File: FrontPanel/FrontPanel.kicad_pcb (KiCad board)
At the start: 2 copper layers, 66 parts, among them SW1 Channel 1, SW10 5, SW11 2, SW12 0, SW13 9, SW14 6, SW15 3, SW16 Backspace, SW17 Voltage 1, SW18 Current 1, SW19 Voltage 2, SW2 Confirm, SW20 Current 2, SW3 Cancel, SW4 Channel 2, SW5 7, SW6 4, SW7 1, SW8 Decimal, SW9 8

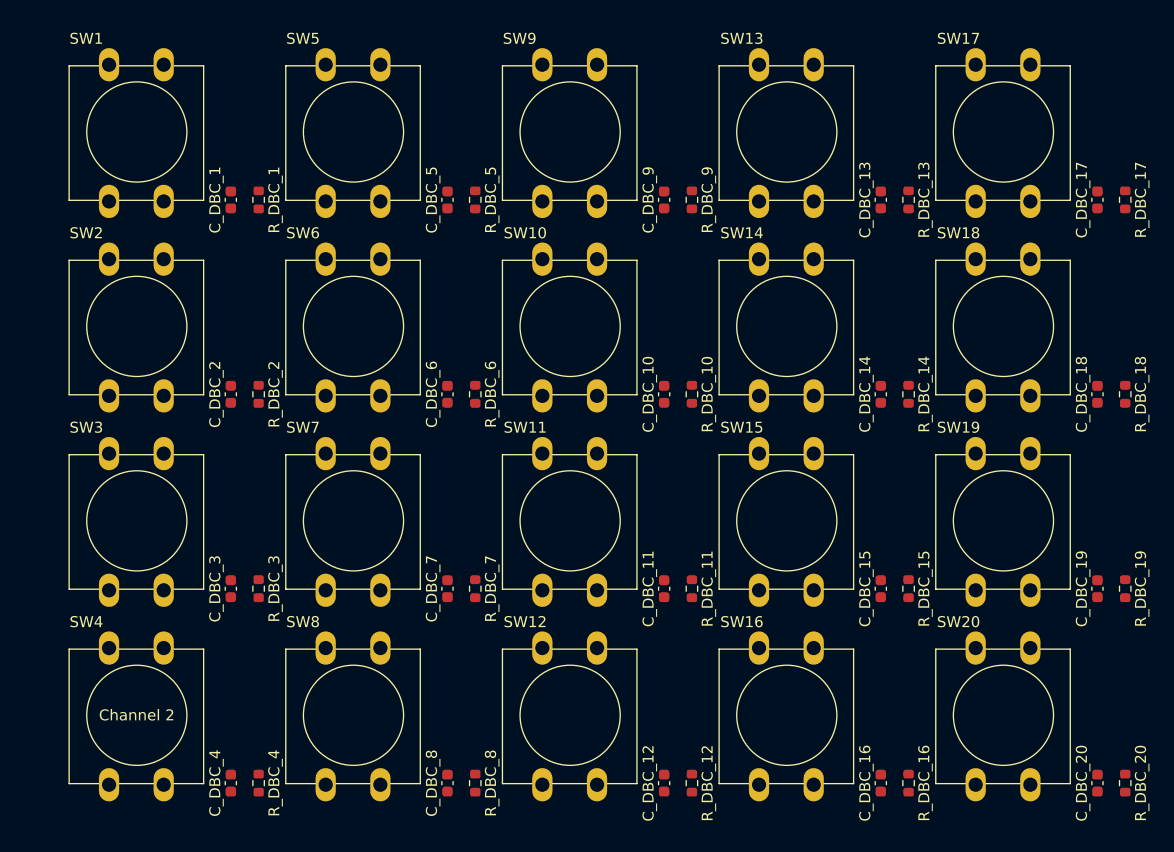
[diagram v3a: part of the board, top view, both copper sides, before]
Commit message: Compressed keypad
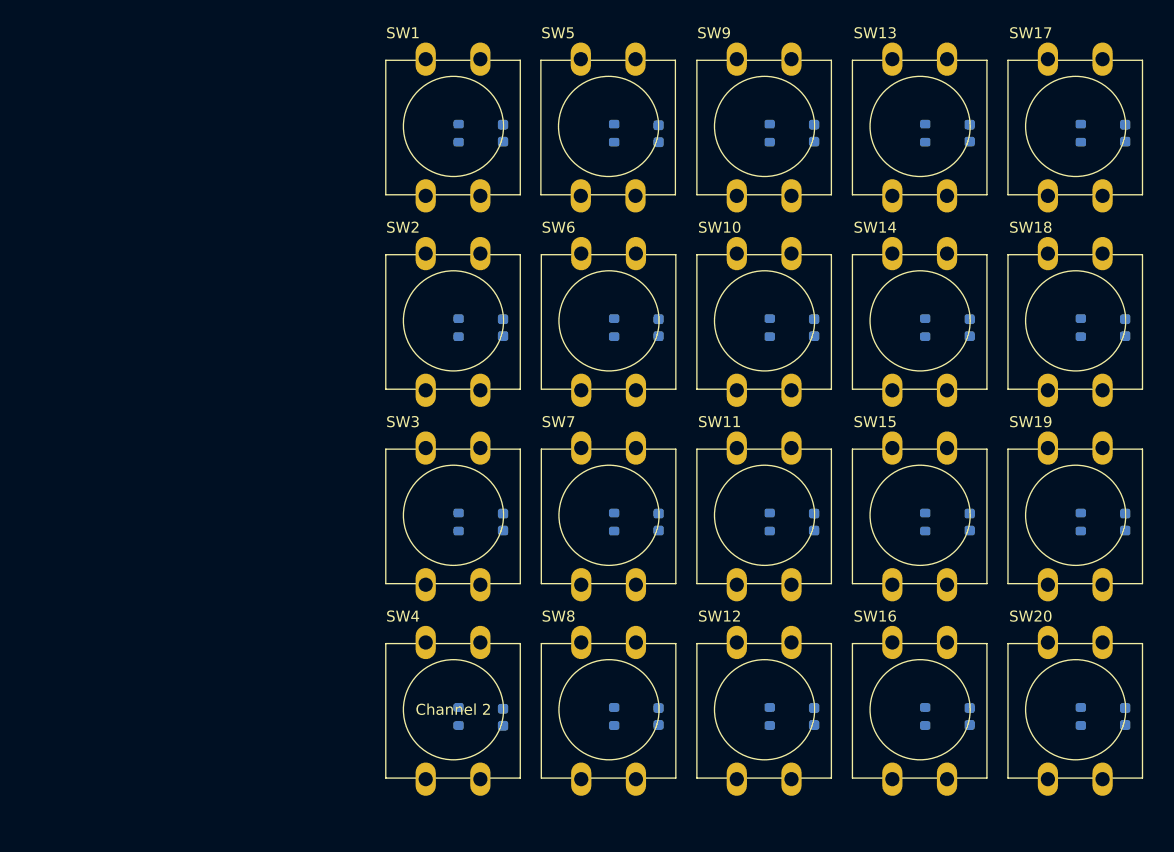
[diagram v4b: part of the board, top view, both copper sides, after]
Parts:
- C_DBC_1, C_DBC_10, C_DBC_11, C_DBC_12, C_DBC_13, C_DBC_14, C_DBC_15, C_DBC_16, C_DBC_17, C_DBC_18, C_DBC_19, C_DBC_2, C_DBC_20, C_DBC_3, C_DBC_4, C_DBC_5, C_DBC_6, C_DBC_7, C_DBC_8, C_DBC_9, R_DBC_1, R_DBC_10, R_DBC_11, R_DBC_12, R_DBC_13, R_DBC_14, R_DBC_15, R_DBC_16, R_DBC_17, R_DBC_18, R_DBC_19, R_DBC_2, R_DBC_20, R_DBC_3, R_DBC_4, R_DBC_5, R_DBC_6, R_DBC_7, R_DBC_8, R_DBC_9: moved to B.Cu
- moved SW1 29.0 mm to (215.9, 29.6)
- moved SW2 29.0 mm to (215.9, 47.4)
- moved SW3 29.0 mm to (215.9, 65.2)
- moved SW4 29.0 mm to (215.9, 82.9)
- moved C_DBC_1 25.6 mm to (223.0, 23.9), turned to -90 degrees
- moved C_DBC_2 25.6 mm to (223.0, 41.7), turned to -90 degrees
- moved C_DBC_3 25.6 mm to (223.0, 59.4), turned to -90 degrees
- moved C_DBC_4 25.6 mm to (223.0, 77.3), turned to -90 degrees
- moved SW6 23.4 mm to (230.2, 47.4)
- moved SW7 23.4 mm to (230.2, 65.2)
- moved SW8 23.4 mm to (230.2, 82.9)
- moved SW5 23.3 mm to (230.1, 29.6)
- moved C_DBC_6 20.2 mm to (237.2, 41.7), turned to -90 degrees
- moved C_DBC_8 20.2 mm to (237.2, 77.2), turned to -90 degrees
- moved C_DBC_7 20.2 mm to (237.2, 59.4), turned to -90 degrees
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
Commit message: Front Panel
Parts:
- removed R1_LED1, R1_LED2: 100, Resistor_SMD:R_0603_1608Metric
- added C_DBC_21: 100n, Capacitor_SMD:C_0603_1608Metric, B.Cu at (186.8, 47.4)
- added C_DBC_22: 100n, Capacitor_SMD:C_0603_1608Metric, B.Cu at (186.8, 52.5)
- added C_DBC_23: 100n, Capacitor_SMD:C_0603_1608Metric, B.Cu at (183.8, 48.3)
- added R1: 100, Resistor_SMD:R_0603_1608Metric, F.Cu at (159.1, 37.2)
- added R2: 100, Resistor_SMD:R_0603_1608Metric, F.Cu at (159.1, 62.9)
- added R_DBC_21: 1k, Resistor_SMD:R_0603_1608Metric, B.Cu at (190.6, 41.1)
- added R_DBC_22: 1k, Resistor_SMD:R_0603_1608Metric, B.Cu at (190.6, 58.7)
- added R_DBC_23: 1k, Resistor_SMD:R_0603_1608Metric, B.Cu at (179.5, 48.3)
- Power1, Power2: footprint LED_THT:LED_D3.0mm -> LED_SMD:LED_0603_1608Metric
- moved Front_Panel2 184.4 mm to (200.9, 58.8), turned to 0 degrees
- moved RotaryEncoder+Switch1 158.7 mm to (190.6, 52.4), turned to 180 degrees
- moved Power2 131.8 mm to (163.4, 62.9)
- moved Power1 119.9 mm to (163.4, 37.2)
- moved C_DBC_1 55.0 mm to (168.0, 23.9)
- moved C_DBC_4 55.0 mm to (168.0, 77.3)
- moved R_DBC_1 55.0 mm to (164.0, 23.9)
- moved R_DBC_4 55.0 mm to (164.0, 77.2)
- moved SW1 55.0 mm to (160.9, 29.6)
- moved SW4 55.0 mm to (160.9, 82.9)
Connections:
- C_DBC_1 pad 2: Net-(C_DBC_2-Pad2) -> Net-(C_DBC_1-Pad2)
- C_DBC_10 pad 2: Net-(Front_Panel2-Pad14) -> Net-(C_DBC_10-Pad2)
- C_DBC_11 pad 2: Net-(Front_Panel2-Pad14) -> Net-(C_DBC_10-Pad2)
- C_DBC_12 pad 2: Net-(Front_Panel2-Pad14) -> Net-(C_DBC_10-Pad2)
- C_DBC_13 pad 2: Net-(Front_Panel2-Pad13) -> Net-(C_DBC_13-Pad2)
- C_DBC_14 pad 2: Net-(Front_Panel2-Pad13) -> Net-(C_DBC_13-Pad2)
- C_DBC_15 pad 2: Net-(Front_Panel2-Pad13) -> Net-(C_DBC_13-Pad2)
- C_DBC_16 pad 2: Net-(Front_Panel2-Pad13) -> Net-(C_DBC_13-Pad2)
- C_DBC_17 pad 2: Net-(Front_Panel2-Pad12) -> Net-(C_DBC_17-Pad2)
- C_DBC_18 pad 2: Net-(Front_Panel2-Pad12) -> Net-(C_DBC_17-Pad2)
- C_DBC_19 pad 2: Net-(Front_Panel2-Pad12) -> Net-(C_DBC_17-Pad2)
- C_DBC_2 pad 2: Net-(C_DBC_2-Pad2) -> Net-(C_DBC_1-Pad2)
- C_DBC_20 pad 2: Net-(Front_Panel2-Pad12) -> Net-(C_DBC_17-Pad2)
- C_DBC_3 pad 2: Net-(C_DBC_2-Pad2) -> Net-(C_DBC_1-Pad2)
- C_DBC_4 pad 2: Net-(C_DBC_2-Pad2) -> Net-(C_DBC_1-Pad2)
- C_DBC_5 pad 2: Net-(Front_Panel2-Pad15) -> Net-(C_DBC_5-Pad2)
- C_DBC_6 pad 2: Net-(Front_Panel2-Pad15) -> Net-(C_DBC_5-Pad2)
- C_DBC_7 pad 2: Net-(Front_Panel2-Pad15) -> Net-(C_DBC_5-Pad2)
- C_DBC_8 pad 2: Net-(Front_Panel2-Pad15) -> Net-(C_DBC_5-Pad2)
- C_DBC_9 pad 2: Net-(Front_Panel2-Pad14) -> Net-(C_DBC_10-Pad2)
- Front_Panel2 pad 1: /3.3 Volts -> Net-(Front_Panel2-Pad1)
- Front_Panel2 pad 10: Net-(Front_Panel2-Pad10) -> Net-(C_DBC_13-Pad2)
- Front_Panel2 pad 11: Net-(Front_Panel2-Pad11) -> Net-(C_DBC_17-Pad2)
- Front_Panel2 pad 12: Net-(Front_Panel2-Pad12) -> unconnected-(Front_Panel2-Pad12)
- Front_Panel2 pad 13: Net-(Front_Panel2-Pad13) -> Net-(SW1-Pad1)
- Front_Panel2 pad 14: Net-(Front_Panel2-Pad14) -> Net-(SW10-Pad1)
- Front_Panel2 pad 15: Net-(Front_Panel2-Pad15) -> Net-(SW11-Pad1)
- Front_Panel2 pad 16: Net-(C_DBC_2-Pad2) -> Net-(SW12-Pad1)
- Front_Panel2 pad 7: Net-(Front_Panel2-Pad7) -> Net-(C_DBC_1-Pad2)
- Front_Panel2 pad 8: Net-(Front_Panel2-Pad8) -> Net-(C_DBC_5-Pad2)
- Front_Panel2 pad 9: Net-(Front_Panel2-Pad9) -> Net-(C_DBC_10-Pad2)
- Power1 pad 2: Net-(Front_Panel2-Pad6) -> Net-(Front_Panel2-Pad3)
- Power2 pad 2: Net-(Front_Panel2-Pad7) -> Net-(Front_Panel2-Pad2)
- R_DBC_1 pad 1: Net-(C_DBC_2-Pad2) -> Net-(C_DBC_1-Pad2)
- R_DBC_10 pad 1: Net-(Front_Panel2-Pad14) -> Net-(C_DBC_10-Pad2)
- R_DBC_11 pad 1: Net-(Front_Panel2-Pad14) -> Net-(C_DBC_10-Pad2)
- R_DBC_12 pad 1: Net-(Front_Panel2-Pad14) -> Net-(C_DBC_10-Pad2)
- R_DBC_13 pad 1: Net-(Front_Panel2-Pad13) -> Net-(C_DBC_13-Pad2)
- R_DBC_14 pad 1: Net-(Front_Panel2-Pad13) -> Net-(C_DBC_13-Pad2)
- R_DBC_15 pad 1: Net-(Front_Panel2-Pad13) -> Net-(C_DBC_13-Pad2)
- R_DBC_16 pad 1: Net-(Front_Panel2-Pad13) -> Net-(C_DBC_13-Pad2)
- R_DBC_17 pad 1: Net-(Front_Panel2-Pad12) -> Net-(C_DBC_17-Pad2)
- R_DBC_18 pad 1: Net-(Front_Panel2-Pad12) -> Net-(C_DBC_17-Pad2)
- R_DBC_19 pad 1: Net-(Front_Panel2-Pad12) -> Net-(C_DBC_17-Pad2)
- R_DBC_2 pad 1: Net-(C_DBC_2-Pad2) -> Net-(C_DBC_1-Pad2)
- R_DBC_20 pad 1: Net-(Front_Panel2-Pad12) -> Net-(C_DBC_17-Pad2)
- R_DBC_3 pad 1: Net-(C_DBC_2-Pad2) -> Net-(C_DBC_1-Pad2)
- R_DBC_4 pad 1: Net-(C_DBC_2-Pad2) -> Net-(C_DBC_1-Pad2)
- R_DBC_5 pad 1: Net-(Front_Panel2-Pad15) -> Net-(C_DBC_5-Pad2)
- R_DBC_6 pad 1: Net-(Front_Panel2-Pad15) -> Net-(C_DBC_5-Pad2)
- R_DBC_7 pad 1: Net-(Front_Panel2-Pad15) -> Net-(C_DBC_5-Pad2)
- R_DBC_8 pad 1: Net-(Front_Panel2-Pad15) -> Net-(C_DBC_5-Pad2)
- R_DBC_9 pad 1: Net-(Front_Panel2-Pad14) -> Net-(C_DBC_10-Pad2)
- RotaryEncoder+Switch1 pad A: /3.3 Volts -> Net-(RotaryEncoder+Switch1-PadA)
- RotaryEncoder+Switch1 pad B: Net-(Front_Panel2-Pad5) -> Net-(R_DBC_21-Pad2)
- RotaryEncoder+Switch1 pad C: Net-(Front_Panel2-Pad4) -> Net-(Front_Panel2-Pad1)
- RotaryEncoder+Switch1 pad S1: Net-(Front_Panel2-Pad2) -> Net-(Front_Panel2-Pad6)
- RotaryEncoder+Switch1 pad S2: Net-(Front_Panel2-Pad3) -> Net-(Front_Panel2-Pad1)
- SW1 pad 1: Net-(Front_Panel2-Pad11) -> Net-(SW1-Pad1)
- SW1 pad 2: Net-(C_DBC_2-Pad2) -> Net-(C_DBC_1-Pad2)
- SW10 pad 1: Net-(Front_Panel2-Pad10) -> Net-(SW10-Pad1)
- SW10 pad 2: Net-(Front_Panel2-Pad14) -> Net-(C_DBC_10-Pad2)
- SW11 pad 1: Net-(Front_Panel2-Pad9) -> Net-(SW11-Pad1)
- SW11 pad 2: Net-(Front_Panel2-Pad14) -> Net-(C_DBC_10-Pad2)
- SW12 pad 1: Net-(Front_Panel2-Pad8) -> Net-(SW12-Pad1)
- SW12 pad 2: Net-(Front_Panel2-Pad14) -> Net-(C_DBC_10-Pad2)
- SW13 pad 1: Net-(Front_Panel2-Pad11) -> Net-(SW1-Pad1)
- SW13 pad 2: Net-(Front_Panel2-Pad13) -> Net-(C_DBC_13-Pad2)
- SW14 pad 1: Net-(Front_Panel2-Pad10) -> Net-(SW10-Pad1)
- SW14 pad 2: Net-(Front_Panel2-Pad13) -> Net-(C_DBC_13-Pad2)
- SW15 pad 1: Net-(Front_Panel2-Pad9) -> Net-(SW11-Pad1)
- SW15 pad 2: Net-(Front_Panel2-Pad13) -> Net-(C_DBC_13-Pad2)
- SW16 pad 1: Net-(Front_Panel2-Pad8) -> Net-(SW12-Pad1)
- SW16 pad 2: Net-(Front_Panel2-Pad13) -> Net-(C_DBC_13-Pad2)
- SW17 pad 1: Net-(Front_Panel2-Pad11) -> Net-(SW1-Pad1)
- SW17 pad 2: Net-(Front_Panel2-Pad12) -> Net-(C_DBC_17-Pad2)
- SW18 pad 1: Net-(Front_Panel2-Pad10) -> Net-(SW10-Pad1)
- SW18 pad 2: Net-(Front_Panel2-Pad12) -> Net-(C_DBC_17-Pad2)
- SW19 pad 1: Net-(Front_Panel2-Pad9) -> Net-(SW11-Pad1)
- SW19 pad 2: Net-(Front_Panel2-Pad12) -> Net-(C_DBC_17-Pad2)
- SW2 pad 1: Net-(Front_Panel2-Pad10) -> Net-(SW10-Pad1)
- SW2 pad 2: Net-(C_DBC_2-Pad2) -> Net-(C_DBC_1-Pad2)
- SW20 pad 1: Net-(Front_Panel2-Pad8) -> Net-(SW12-Pad1)
- SW20 pad 2: Net-(Front_Panel2-Pad12) -> Net-(C_DBC_17-Pad2)
- SW3 pad 1: Net-(Front_Panel2-Pad9) -> Net-(SW11-Pad1)
- SW3 pad 2: Net-(C_DBC_2-Pad2) -> Net-(C_DBC_1-Pad2)
- SW4 pad 1: Net-(Front_Panel2-Pad8) -> Net-(SW12-Pad1)
- SW4 pad 2: Net-(C_DBC_2-Pad2) -> Net-(C_DBC_1-Pad2)
- SW5 pad 1: Net-(Front_Panel2-Pad11) -> Net-(SW1-Pad1)
- SW5 pad 2: Net-(Front_Panel2-Pad15) -> Net-(C_DBC_5-Pad2)
- SW6 pad 1: Net-(Front_Panel2-Pad10) -> Net-(SW10-Pad1)
- SW6 pad 2: Net-(Front_Panel2-Pad15) -> Net-(C_DBC_5-Pad2)
- SW7 pad 1: Net-(Front_Panel2-Pad9) -> Net-(SW11-Pad1)
- SW7 pad 2: Net-(Front_Panel2-Pad15) -> Net-(C_DBC_5-Pad2)
- SW8 pad 1: Net-(Front_Panel2-Pad8) -> Net-(SW12-Pad1)
- SW8 pad 2: Net-(Front_Panel2-Pad15) -> Net-(C_DBC_5-Pad2)
- SW9 pad 1: Net-(Front_Panel2-Pad11) -> Net-(SW1-Pad1)
- SW9 pad 2: Net-(Front_Panel2-Pad14) -> Net-(C_DBC_10-Pad2)

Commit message: Squeezed front panel
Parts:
- moved C_DBC_1 20.1 mm to (188.1, 23.9)
- moved C_DBC_4 20.1 mm to (188.1, 77.3)
- moved R1 20.1 mm to (179.2, 37.2)
- moved R2 20.1 mm to (179.2, 62.9)
- moved R_DBC_1 20.1 mm to (184.0, 23.9)
- moved R_DBC_4 20.1 mm to (184.0, 77.2)
- moved Power1 20.1 mm to (183.5, 37.2)
- moved Power2 20.1 mm to (183.5, 62.9)
- moved SW1 20.1 mm to (181.0, 29.6)
- moved SW4 20.1 mm to (181.0, 82.9)
- moved C_DBC_2 17.8 mm to (223.0, 23.9)
- moved R_DBC_2 17.8 mm to (218.9, 23.9)
- moved SW2 17.8 mm to (215.9, 29.6)
- moved C_DBC_3 17.8 mm to (223.0, 77.2)
- moved R_DBC_3 17.8 mm to (218.9, 77.2)
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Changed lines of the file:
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@@
   )
   (footprint "Button_Switch_THT:SW_PUSH-12mm" (layer "F.Cu")
-    (at 215.94 65.168 90)
+    (at 215.94 82.948 90)
     (descr "SW PUSH 12mm https://www.e-switch.com/system/asset/product_line/data_sheet/143/TL1100.pdf")
     (tags "tact sw push 12mm")
@@
   )
   (footprint "Resistor_SMD:R_0603_1608Metric" (layer "F.Cu")
-    (at 159.131 37.211)
+    (at 179.197 37.211)
     (descr "Resistor SMD 0603 (1608 Metric), square (rectangular) end terminal, IPC_7351 nominal, (Body size source: IPC-SM-782 page 72, https://www.pcb-3d.com/wordpress/wp-content/uploads/ipc-sm-782a_amendment_1_and_2.pdf), generated with kicad-footprint-generator")
     (tags "resistor")
@@
   )
   (footprint "LED_SMD:LED_0603_1608Metric" (layer "F.Cu")
-    (at 163.449 37.211)
+    (at 183.515 37.211)
     (descr "LED SMD 0603 (1608 Metric), square (rectangular) end terminal, IPC_7351 nominal, (Body size source: http://www.tortai-tech.com/upload/download/2011102023233369053.pdf), generated with kicad-footprint-generator")
     (tags "LED")
@@
   )
   (footprint "LED_SMD:LED_0603_1608Metric" (layer "F.Cu")
-    (at 163.449 62.865)
+    (at 183.515 62.865)
     (descr "LED SMD 0603 (1608 Metric), square (rectangular) end terminal, IPC_7351 nominal, (Body size source: http://www.tortai-tech.com/upload/download/2011102023233369053.pdf), generated with kicad-footprint-generator")
     (tags "LED")
@@
   )
   (footprint "Rotary_Encoder:RotaryEncoder_Alps_EC11E-Switch_Vertical_H20mm" (layer "F.Cu")
-    (at 190.627 52.411 180)
+    (at 208.28 52.411 180)
     (descr "Alps rotary encoder, EC12E... with switch, vertical shaft, http://www.alps.com/prod/info/E/HTML/Encoder/Incremental/EC11/EC11E15204A3.html")
     (tags "rotary encoder")
@@
   )
   (footprint "Button_Switch_THT:SW_PUSH-12mm" (layer "F.Cu")
-    (at 160.949 29.608 90)
+    (at 181.015 29.608 90)
     (descr "SW PUSH 12mm https://www.e-switch.com/system/asset/product_line/data_sheet/143/TL1100.pdf")
     (tags "tact sw push 12mm")
@@
   )
   (footprint "Button_Switch_THT:SW_PUSH-12mm" (layer "F.Cu")
-    (at 215.94 47.388 90)
+    (at 215.94 29.608 90)
     (descr "SW PUSH 12mm https://www.e-switch.com/system/asset/product_line/data_sheet/143/TL1100.pdf")
     (tags "tact sw push 12mm")
@@
   )
   (footprint "Resistor_SMD:R_0603_1608Metric" (layer "F.Cu")
-    (at 159.131 62.865)
+    (at 179.197 62.865)
     (descr "Resistor SMD 0603 (1608 Metric), square (rectangular) end terminal, IPC_7351 nominal, (Body size source: IPC-SM-782 page 72, https://www.pcb-3d.com/wordpress/wp-content/uploads/ipc-sm-782a_amendment_1_and_2.pdf), generated with kicad-footprint-generator")
     (tags "resistor")
@@
   )
   (footprint "Button_Switch_THT:SW_PUSH-12mm" (layer "F.Cu")
-    (at 160.949 82.948 90)
+    (at 181.015 82.948 90)
     (descr "SW PUSH 12mm https://www.e-switch.com/system/asset/product_line/data_sheet/143/TL1100.pdf")
     (tags "tact sw push 12mm")
@@
   )
   (footprint "Capacitor_SMD:C_0603_1608Metric" (layer "B.Cu")
-    (at 223.012 59.436 -90)
+    (at 223.012 77.216 -90)
     (descr "Capacitor SMD 0603 (1608 Metric), square (rectangular) end terminal, IPC_7351 nominal, (Body size source: IPC-SM-782 page 76, https://www.pcb-3d.com/wordpress/wp-content/uploads/ipc-sm-782a_amendment_1_and_2.pdf), generated with kicad-footprint-generator")
     (tags "capacitor")
@@
   )
   (footprint "Capacitor_SMD:C_0603_1608Metric" (layer "B.Cu")
-    (at 223.012 41.656 -90)
+    (at 223.012 23.876 -90)
     (descr "Capacitor SMD 0603 (1608 Metric), square (rectangular) end terminal, IPC_7351 nominal, (Body size source: IPC-SM-782 page 76, https://www.pcb-3d.com/wordpress/wp-content/uploads/ipc-sm-782a_amendment_1_and_2.pdf), generated with kicad-footprint-generator")
     (tags "capacitor")
@@
   )
   (footprint "Resistor_SMD:R_0603_1608Metric" (layer "B.Cu")
-    (at 163.957 77.216 90)
+    (at 184.023 77.216 90)
     (descr "Resistor SMD 0603 (1608 Metric), square (rectangular) end terminal, IPC_7351 nominal, (Body size source: IPC-SM-782 page 72, https://www.pcb-3d.com/wordpress/wp-content/uploads/ipc-sm-782a_amendment_1_and_2.pdf), generated with kicad-footprint-generator")
     (tags "resistor")
@@
   )
   (footprint "Capacitor_SMD:C_0603_1608Metric" (layer "B.Cu")
-    (at 183.769 48.26 -90)
+    (at 201.422 48.26 -90)
     (descr "Capacitor SMD 0603 (1608 Metric), square (rectangular) end terminal, IPC_7351 nominal, (Body size source: IPC-SM-782 page 76, https://www.pcb-3d.com/wordpress/wp-content/uploads/ipc-sm-782a_amendment_1_and_2.pdf), generated with kicad-footprint-generator")
     (tags "capacitor")
@@
   )
   (footprint "Resistor_SMD:R_0603_1608Metric" (layer "B.Cu")
-    (at 190.627 41.148 -90)
+    (at 208.28 41.148 -90)
     (descr "Resistor SMD 0603 (1608 Metric), square (rectangular) end terminal, IPC_7351 nominal, (Body size source: IPC-SM-782 page 72, https://www.pcb-3d.com/wordpress/wp-content/uploads/ipc-sm-782a_amendment_1_and_2.pdf), generated with kicad-footprint-generator")
     (tags "resistor")
@@
   )
   (footprint "Resistor_SMD:R_0603_1608Metric" (layer "B.Cu")
-    (at 179.451 48.26 90)
+    (at 197.104 48.26 90)
     (descr "Resistor SMD 0603 (1608 Metric), square (rectangular) end terminal, IPC_7351 nominal, (Body size source: IPC-SM-782 page 72, https://www.pcb-3d.com/wordpress/wp-content/uploads/ipc-sm-782a_amendment_1_and_2.pdf), generated with kicad-footprint-generator")
     (tags "resistor")
@@
   )
   (footprint "Capacitor_SMD:C_0603_1608Metric" (layer "B.Cu")
-    (at 168.021 23.876 -90)
+    (at 188.087 23.876 -90)
     (descr "Capacitor SMD 0603 (1608 Metric), square (rectangular) end terminal, IPC_7351 nominal, (Body size source: IPC-SM-782 page 76, https://www.pcb-3d.com/wordpress/wp-content/uploads/ipc-sm-782a_amendment_1_and_2.pdf), generated with kicad-footprint-generator")
     (tags "capacitor")
@@
   )
   (footprint "Connector_IDC:IDC-Header_2x08_P2.54mm_Vertical" (layer "B.Cu")
-    (at 200.914 58.801)
+    (at 217.1795 58.928)
     (descr "Through hole IDC box header, 2x08, 2.54mm pitch, DIN 41651 / IEC 60603-13, double rows, https://docs.google.com/spreadsheets/d/16SsEcesNF15N3Lb4niX7dcUr-NY5_MFPQhobNuNppn4/edit#gid=0")
     (tags "Through hole vertical IDC box header THT 2x08 2.54mm double row")
@@
   )
   (footprint "Resistor_SMD:R_0603_1608Metric" (layer "B.Cu")
-    (at 163.957 23.876 90)
+    (at 184.023 23.876 90)
     (descr "Resistor SMD 0603 (1608 Metric), square (rectangular) end terminal, IPC_7351 nominal, (Body size source: IPC-SM-782 page 72, https://www.pcb-3d.com/wordpress/wp-content/uploads/ipc-sm-782a_amendment_1_and_2.pdf), generated with kicad-footprint-generator")
     (tags "resistor")
@@
   )
   (footprint "Capacitor_SMD:C_0603_1608Metric" (layer "B.Cu")
-    (at 168.021 77.292 -90)
+    (at 188.087 77.292 -90)
     (descr "Capacitor SMD 0603 (1608 Metric), square (rectangular) end terminal, IPC_7351 nominal, (Body size source: IPC-SM-782 page 76, https://www.pcb-3d.com/wordpress/wp-content/uploads/ipc-sm-782a_amendment_1_and_2.pdf), generated with kicad-footprint-generator")
     (tags "capacitor")
@@
   )
   (footprint "Resistor_SMD:R_0603_1608Metric" (layer "B.Cu")
-    (at 218.948 59.436 90)
+    (at 218.948 77.216 90)
     (descr "Resistor SMD 0603 (1608 Metric), square (rectangular) end terminal, IPC_7351 nominal, (Body size source: IPC-SM-782 page 72, https://www.pcb-3d.com/wordpress/wp-content/uploads/ipc-sm-782a_amendment_1_and_2.pdf), generated with kicad-footprint-generator")
     (tags "resistor")
@@
   )
   (footprint "Capacitor_SMD:C_0603_1608Metric" (layer "B.Cu")
-    (at 186.817 52.451 90)
+    (at 204.47 52.451 90)
     (descr "Capacitor SMD 0603 (1608 Metric), square (rectangular) end terminal, IPC_7351 nominal, (Body size source: IPC-SM-782 page 76, https://www.pcb-3d.com/wordpress/wp-content/uploads/ipc-sm-782a_amendment_1_and_2.pdf), generated with kicad-footprint-generator")
     (tags "capacitor")
@@
   )
   (footprint "Resistor_SMD:R_0603_1608Metric" (layer "B.Cu")
-    (at 218.948 41.656 90)
+    (at 218.948 23.876 90)
     (descr "Resistor SMD 0603 (1608 Metric), square (rectangular) end terminal, IPC_7351 nominal, (Body size source: IPC-SM-782 page 72, https://www.pcb-3d.com/wordpress/wp-content/uploads/ipc-sm-782a_amendment_1_and_2.pdf), generated with kicad-footprint-generator")
     (tags "resistor")
@@
   )
   (footprint "Resistor_SMD:R_0603_1608Metric" (layer "B.Cu")
-    (at 190.627 58.674 -90)
+    (at 208.28 58.674 -90)
     (descr "Resistor SMD 0603 (1608 Metric), square (rectangular) end terminal, IPC_7351 nominal, (Body size source: IPC-SM-782 page 72, https://www.pcb-3d.com/wordpress/wp-content/uploads/ipc-sm-782a_amendment_1_and_2.pdf), generated with kicad-footprint-generator")
     (tags "resistor")
@@
   )
   (footprint "Capacitor_SMD:C_0603_1608Metric" (layer "B.Cu")
-    (at 186.817 47.371 90)
+    (at 204.47 47.371 90)
     (descr "Capacitor SMD 0603 (1608 Metric), square (rectangular) end terminal, IPC_7351 nominal, (Body size source: IPC-SM-782 page 76, https://www.pcb-3d.com/wordpress/wp-content/uploads/ipc-sm-782a_amendment_1_and_2.pdf), generated with kicad-footprint-generator")
     (tags "capacitor")
